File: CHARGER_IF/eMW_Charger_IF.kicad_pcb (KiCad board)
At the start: 2 copper layers, 67 x 129 mm, 13 parts, among them J1 CONN_01X02, J2 Booster_J1_J3, J3 Booster_J4_J2, J5 CONN_02X10, U1 V7805-2000R, U3 SN74ACT08N, U4 SN74ACT08N

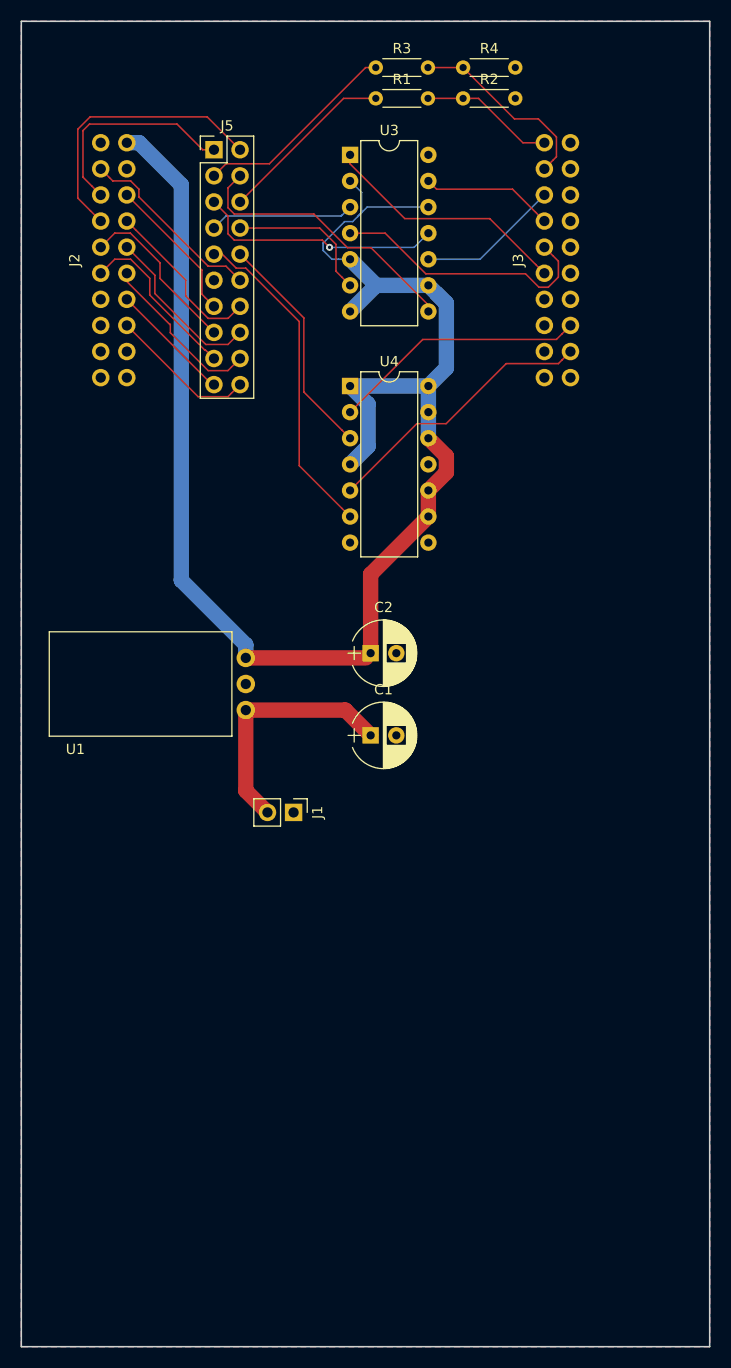
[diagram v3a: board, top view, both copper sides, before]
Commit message: Charger IF
Just need to do a once over before ordering
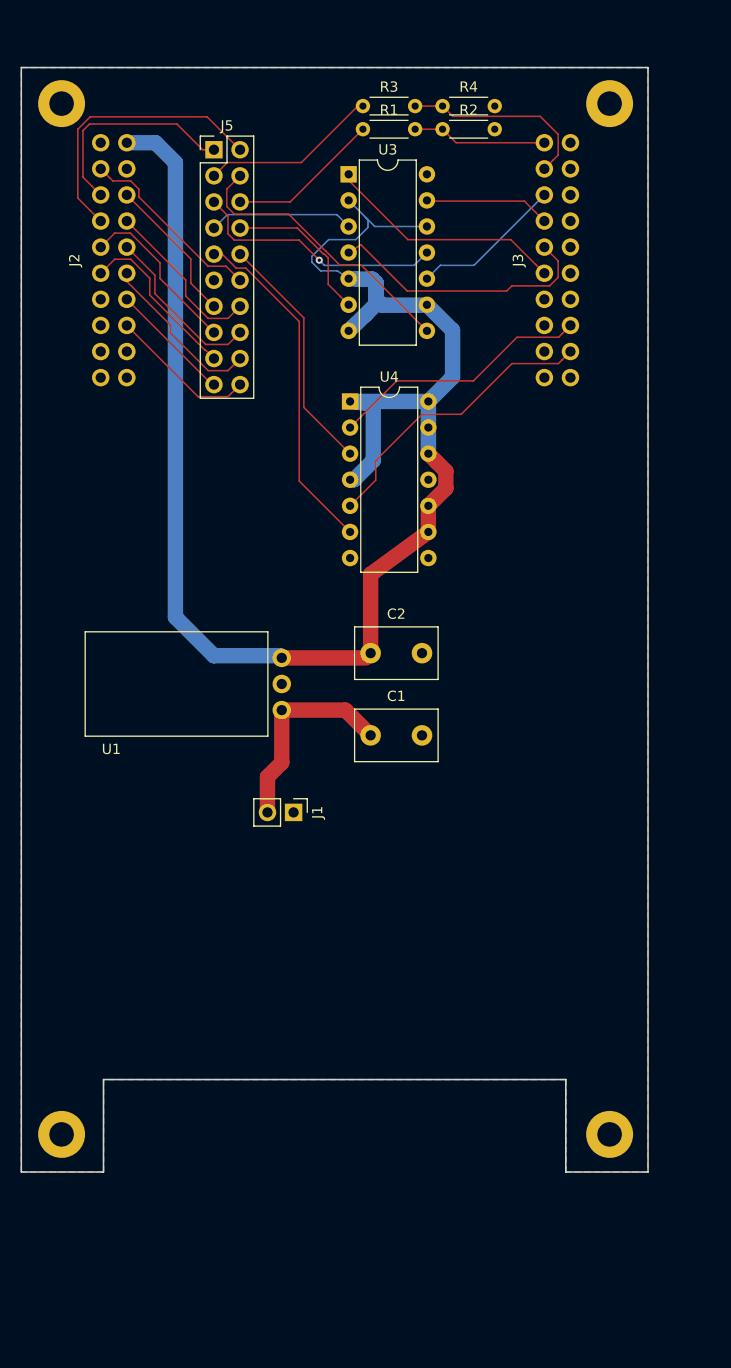
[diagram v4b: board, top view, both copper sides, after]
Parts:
- added REF**: RM57_Mounting_Holes, eMW_Charger:RM57_Mounting_Hole, F.Cu at (107.9, 141.3)
- C1, C2: footprint Capacitors_THT:CP_Radial_D6.3mm_P2.50mm -> Capacitors_THT:C_Disc_D8.0mm_W5.0mm_P5.00mm
- moved R4 4.25 mm to (145.0, 41.2)
- moved R3 3.95 mm to (137.2, 41.2)
- moved R2 3.61 mm to (145.0, 43.5)
- moved U1 3.50 mm to (128.0, 97.5)
- moved R1 3.25 mm to (137.2, 43.5)
- moved U3 1.90 mm to (135.9, 47.9)
- moved U4 1.50 mm to (136.0, 70.0)
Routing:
- net +5V: track 160.0 -> 166.2 mm
- net +12V: track 24.0 -> 20.2 mm
- net Net-(J5-Pad3): track 20.1 -> 17.3 mm
- net Net-(J5-Pad6): track 17.4 -> 14.9 mm
- net Net-(J3-Pad12): track 27.1 -> 28.8 mm
- net Net-(J5-Pad9): track 32.0 -> 33.5 mm
- net Net-(J5-Pad10): track 22.4 -> 23.9 mm
- net Net-(J3-Pad38): track 14.7 -> 15.6 mm
- net Net-(J3-Pad35): track 24.2 -> 23.4 mm
- net Net-(J3-Pad37): track 12.9 -> 12.3 mm
- net Net-(J3-Pad13): track 24.9 -> 25.6 mm
- net Net-(J5-Pad8): track 14.6 -> 15.2 mm
- net Net-(J5-Pad5): track 24.3 -> 24.8 mm
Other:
- board size 67 x 129 mm -> 61 x 107.5 mm

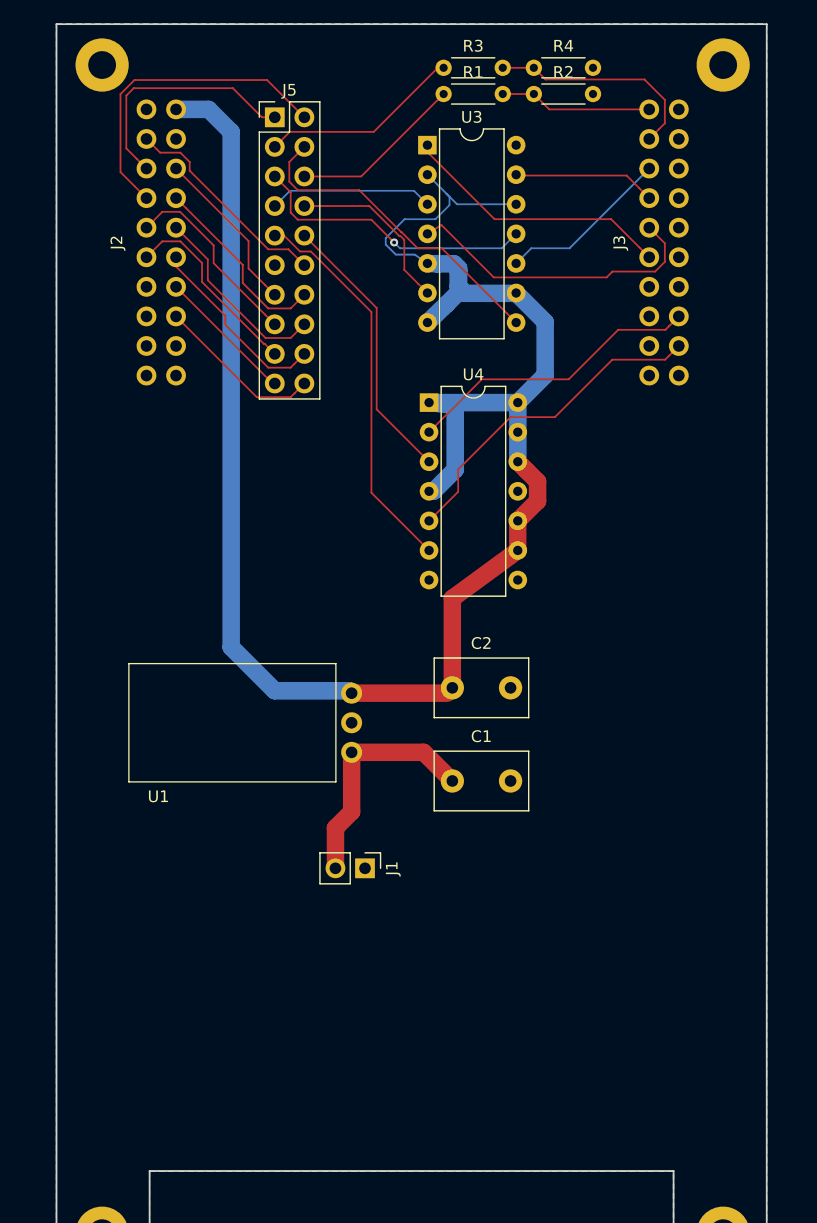
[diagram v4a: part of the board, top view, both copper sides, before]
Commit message: Charger IF
needs double checking and pin labels on silkscreen
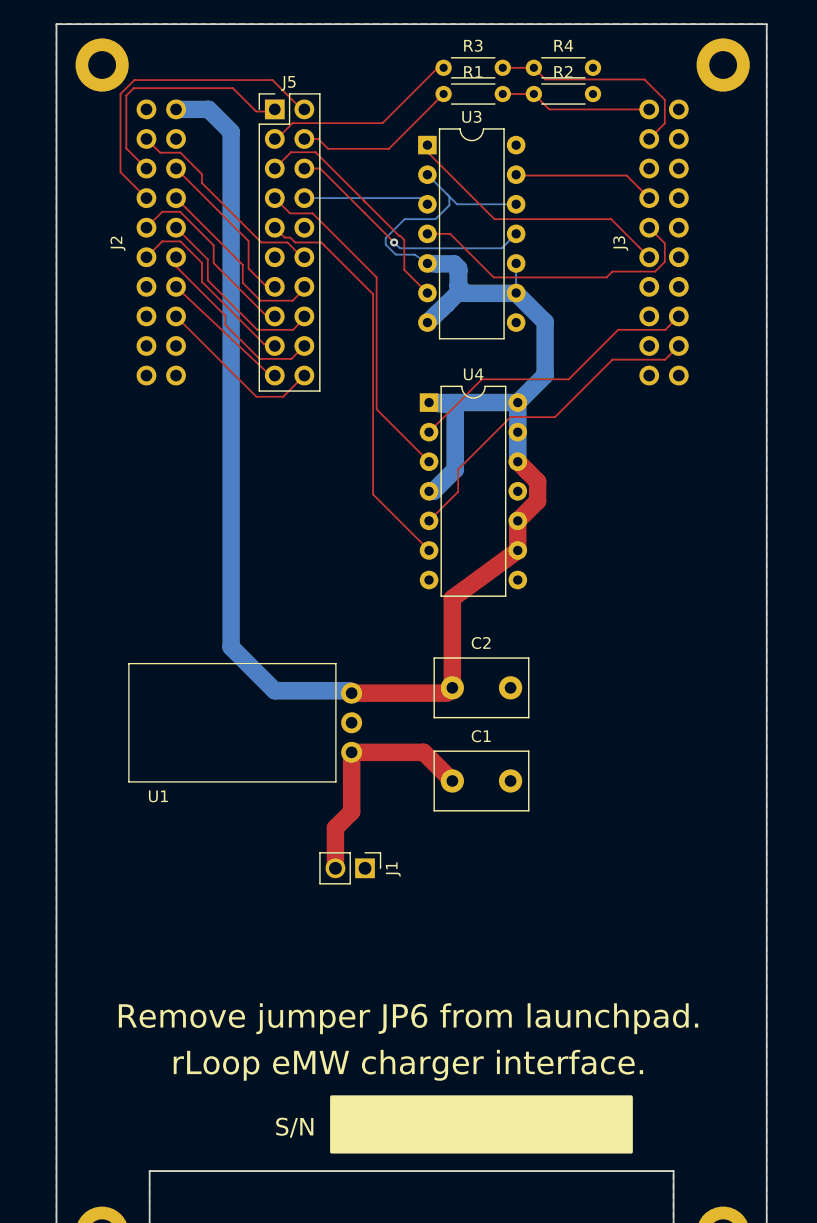
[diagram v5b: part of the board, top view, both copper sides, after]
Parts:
- moved J5 0.68 mm to (122.8, 44.8)
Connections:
- J5 pad 10: Net-(J5-Pad10) -> GND
- R1 pad 1: Net-(J5-Pad6) -> Net-(J5-Pad4)
- U3 pad 10: Net-(J3-Pad38) -> +5V
- U3 pad 11: Net-(J5-Pad5) -> Net-(J5-Pad6)
- U3 pad 3: Net-(J5-Pad7) -> Net-(J5-Pad8)
- U3 pad 6: Net-(J5-Pad8) -> Net-(J5-Pad5)
- U3 pad 8: Net-(J5-Pad4) -> Net-(U3-Pad8)
- U4 pad 3: Net-(J5-Pad10) -> Net-(J5-Pad7)
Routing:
- net Net-(J5-Pad10): track 23.9 -> 0.00 mm
- net Net-(J5-Pad7): track 14.1 -> 29.3 mm
- net Net-(J3-Pad38): track 15.6 -> 0.81 mm
- net Net-(J5-Pad4): track 28.0 -> 14.3 mm
- net Net-(J5-Pad6): track 14.9 -> 21.5 mm, vias 0 -> 1
- net Net-(J5-Pad5): track 24.8 -> 20.4 mm, vias 1 -> 0
- net Net-(J5-Pad8): track 15.2 -> 10.8 mm
- net +5V: track 166.2 -> 168.7 mm
- net Net-(J5-Pad9): track 33.5 -> 34.8 mm
- net Net-(J3-Pad36): track 26.5 -> 26.0 mm
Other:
- board text added: "Remove jumper JP6 from launchpad."
- board text added: "S/N"
- board text added: "rLoop eMW charger interface."

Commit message: Final Charger IF
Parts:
- added J4: CONN_02X10, Pin_Headers:Pin_Header_Straight_2x10_Pitch2.54mm, F.Cu at (134.5, 155.1)
- added U2: Arduino-Socket, eMW_Charger:eMW-Control-Board-Arduino-Header, F.Cu at (134.5, 155.1)
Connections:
- J5 pad 12: Net-(J2-Pad2) -> Net-(J5-Pad12)
- U3 pad 10: +5V -> Net-(J3-Pad38)
- U3 pad 8: Net-(U3-Pad8) -> Net-(J5-Pad12)
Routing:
- net Net-(J5-Pad12): track 0.00 -> 23.2 mm, vias 0 -> 1
- net Net-(J2-Pad2): track 18.6 -> 0.00 mm
- net Net-(J3-Pad38): track 0.81 -> 15.6 mm
- net +5V: track 168.7 -> 166.2 mm
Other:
- board text added: "+"
- board text added: "12V"
- board text added: "A0-C Sense"
- board text added: "A1-V Sense"
- board text added: "A2-H.S. Temp"
- board text added: "A3-Uvio"
- board text added: "A4-Ts"
- board text added: "A5-MainsV"
- board text added: "A6-Th"
- board text added: "A7-bC"
- board text added: "D10-Max C PWM"
- board text added: "D2-Red Btn"
- board text added: "D3-Green Btn"
- board text added: "D4"
- board text added: "D5"
- board text added: "D6-Shutdown"
- board text added: "D8-Fan Relay"
- board text added: "D9-Charge C PWM"
- board text added: "RX"
- board text added: "TX"

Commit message: Finals w/ pdf
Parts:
- removed J4: CONN_02X10, Pin_Headers:Pin_Header_Straight_2x10_Pitch2.54mm
- removed U2: Arduino-Socket, eMW_Charger:eMW-Control-Board-Arduino-Header
